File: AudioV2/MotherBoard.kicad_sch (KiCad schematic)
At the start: 50 parts, among them J201 +15/-15/A_GND out, J202 PD module in (1=GND 2=+12V), SW402 PWR SW, SW501 DEST L (PHONE/MUTE/LINE), SW502 DEST R (PHONE/MUTE/LINE), U201 REC10K-2415DAW/H2, U202 L7809CV +9V, U402 PT2314-D, U403 BP5293-50 +5V

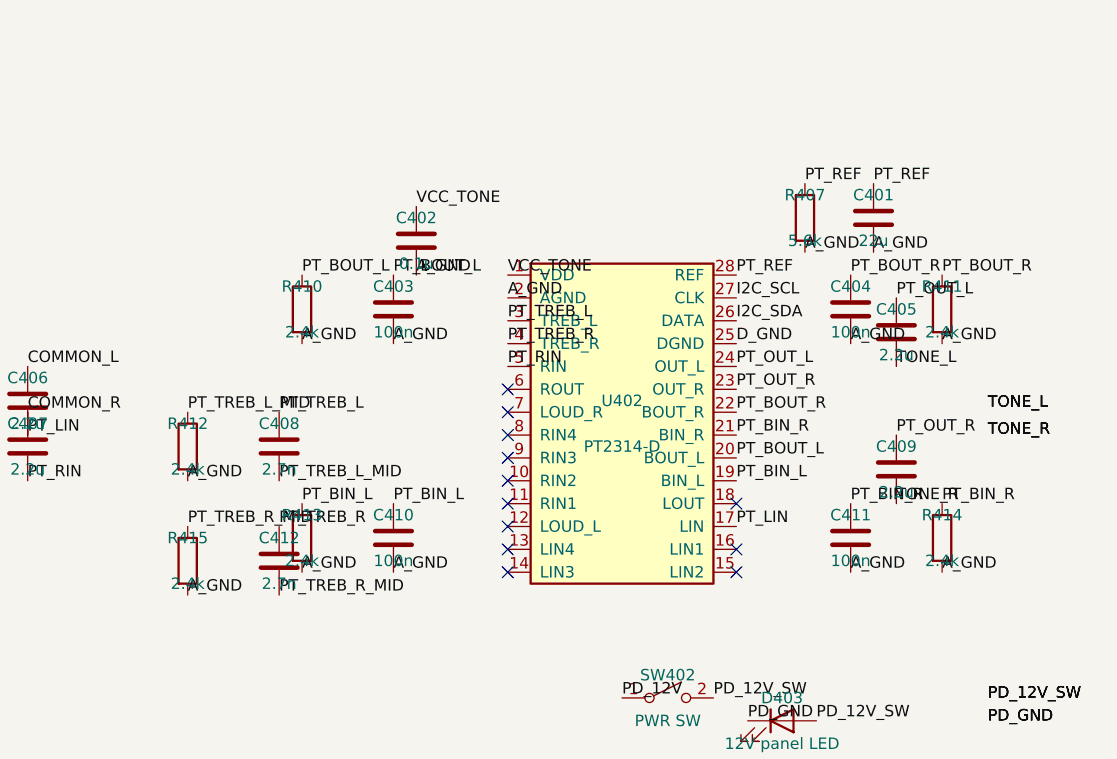
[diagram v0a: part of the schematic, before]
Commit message: AudioV2: PT2314E に切り替え、トーン網をデータシート通りに組み直した
無印 PT2314 は DigiKey に在庫が無く（フォーラムでモデレータ自身が調達困難と
回答し TDA7440 を代替に挙げている）、LCSC / JLCPCB にあるのは PT2314E のみ。
E は "Improved and replace PT2314 and PT2314A" と明記され、28ピンの名前・番号は
無印と完全一致（I2C の 26/27 が DATA/CLK -> SDA/SCL に改名されただけ）。

切り替えにあたって外付け網をデータシートと突き合わせたところ、3箇所ずれていた。
値の一覧は合っていたが置き場所が入れ替わっていた。2.4k は本来「使わないセレクタ
入力の直列抵抗」、5.6k は「低音網の集約点」。

  低音  DS: BOUT -[100n]-+-[5.6k]- GND
                BIN  -[100n]-+          （1点に集約）
        旧: BOUT/BIN が各自 100n と 2.4k で別々に GND。集約点が無く
            BIN->BASS->BOUT の外付け帰還路が成立していなかった
  高音  DS: TREB -[2.7n]- GND
        旧: TREB -[2.7n]-[2.4k]- GND（直列抵抗が余分）
  REF   DS: REF -[22u]- GND
        旧: REF -[22u]- GND に加えて 5.6k で GND へ（内部基準を引いていた）

無印 PT2314 のアプリケーション回路も同じ網なので、E への切り替えとは独立の誤り。

素材 legacy/ControlPanelAnalog.kicad_sch を編集して再生成した。この素材は
ワイヤを持たずラベルをピン先へ直置きする方式なので、配線変更はラベルの
張り替えで足りる。prune() は使っていない（このシートでもラベルを浮きと
誤認して落とすため）。消した部品のラベルはピン先座標で特定して消した。

  R410/R411  2.4k -> 5.6k、集約点 PT_BASS_L/R へ移動
  R407/R412/R413/R414/R415  削除
  C403/C410/C404/C411  GND 側を集約点へ
  C408/C412  中間ノードをやめて直接 A_GND へ
  U402 Value  PT2314-D -> PT2314E

フットプリントは設定していない。SOP-28 300mil だが、入手したDS抜粋に外形寸法が
無く SOIC-28W_7.5x17.9 と 7.5x18.7 のどちらか決められない。誤った値を入れると
「未設定」という目印が消えるので B5 で実物を見てから付ける。

検証:
  erc         17 件（変化なし。新規違反なし）
  netlist     部品 369 / 重複 0（抵抗5本減で 374 -> 369）
  dangling    0 本
  check_sexpr 13 ファイル / 問題 0
  roundtrip   6/6 OK
  再生成      2回目でバイト一致

CLAUDE.md の期待値表と NOW.md も更新した。

Co-Authored-By: Claude Opus 5 <noreply@anthropic.com>
Claude-Session: https://claude.ai/code/session_01VCArLcCGbMGgxvWJ5HFJiY
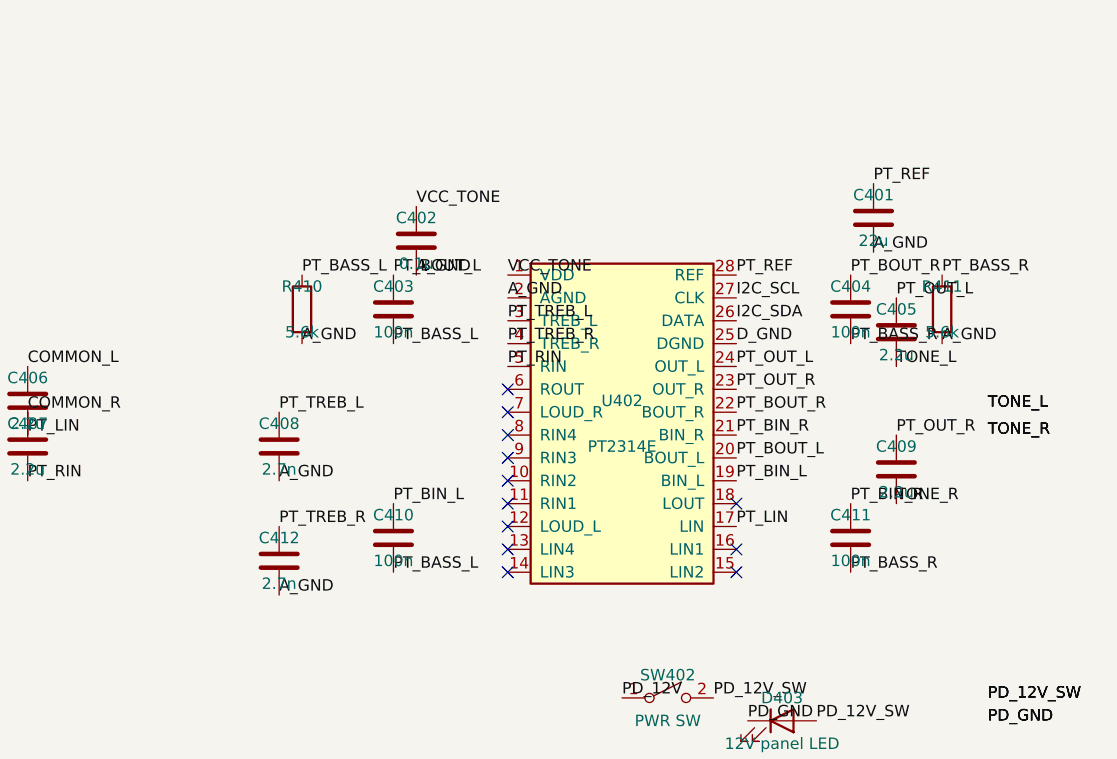
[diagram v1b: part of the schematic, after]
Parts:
- removed R407: 5.6k, symbol Device:R
- removed R412, R413, R414, R415: 2.4k, symbol Device:R
- R410, R411: value 2.4k -> 5.6k
- U402: value PT2314-D -> PT2314E
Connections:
- net PT_TREB_L_MID is gone; now on net A_GND: C408.2
- net PT_TREB_R_MID is gone; now on net A_GND: C412.2
- net A_GND: no longer C403.2, C404.2, C410.2, C411.2
- net PT_BOUT_L: no longer R410.1
- net PT_BOUT_R: no longer R411.1
- new net PT_BASS_L: C403.2, C410.2, R410.1
- new net PT_BASS_R: C404.2, C411.2, R411.1

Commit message: AudioV2: U402 のフットプリントを SOIC-28W_7.5x17.9mm に設定した
JLCPCB の Footprint Manager が出す LCSC の型は
SOP-28_L17.9-W7.5-P1.27-LS10.3 で、外形 17.9 x 7.5・ピッチ 1.27。
KiCad の Package_SO:SOIC-28W_7.5x17.9mm_P1.27mm と一致する。

パッドの伸ばし方だけ違うが、どちらもリードスパン 10.3mm を覆う:

            パッド中心間   パッド寸法      覆う範囲(x)
  LCSC      9.915          0.630 x 1.615   4.150 .. 5.765
  KiCad     9.300          0.600 x 2.050   3.625 .. 5.675
  リード足                                 約 4.35 .. 5.15

KiCad 側は IPC-7351 準拠でヒール側が広い。実装性はどちらでも問題ない。

フットプリント未設定は 45 -> 39。内訳は U402 を設定したぶん 1 個と、
前のコミットで消した抵抗 5 本（R407/R412/R413/R414/R415）がいずれも
未設定組だったぶん。

検証:
  erc         17 件（変化なし）
  netlist     部品 369 / 重複 0（変化なし）
  check_sexpr 13 ファイル / 問題 0
  roundtrip   6/6 OK

Co-Authored-By: Claude Opus 5 <noreply@anthropic.com>
Claude-Session: https://claude.ai/code/session_01VCArLcCGbMGgxvWJ5HFJiY
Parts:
- U402: footprint (none) -> Package_SO:SOIC-28W_7.5x17.9mm_P1.27mm
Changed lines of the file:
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@@
 			)
 		)
-		(property "Footprint" ""
+		(property "Footprint" "Package_SO:SOIC-28W_7.5x17.9mm_P1.27mm"
 			(at 355.6 0 0)
 			(hide yes)

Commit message: AudioV2: 母板のフットプリント 23 個を設計内の前例に合わせて埋めた（39 -> 16）
B5 の下ごしらえ。前例のあるものだけを埋め、判断が要るものには触っていない。

  積セラ 1206     C202/204/206/208/402, C403/404/410/411, C408/412
                  設計で 85 回使われている流儀に合わせた
  抵抗 1206       R410/411（同 128 回）
  フィルム        C405/406/407/409（2.2u）
                  PT2314 の入出力結合で音声が通る。設計内の C601「2.2uF film」と
                  同じ footprint に揃えた。セラミックは電圧で容量が変わるので
                  結合位置に置くと歪む（ユーザー判断 2026-09-07）
  電解            C201/205/207(47u) -> D8.0/P3.50（C1610・C1621 と同じ）
                  C401(22u)         -> D6.3/P2.50（C1630 と同じ）
                  C203(10u)         -> D5.0/P2.00（C1635「10uF 50V」と同じ）
  DC-DC           U403 -> Library:BP5293-50_ROHM_SIP-3
                  U1607 が同一部品で同じ footprint

素材（legacy/ControlPanelAnalog 15個・legacy/PowerModule 8個）を編集して再生成した。

**残り 16 個には触っていない。** 性質が2つに分かれる:

  パネル部品 6（RV501/502・SW501/502/1601・SW402）
    KiCad にもプロジェクトの Audio/Library.pretty にも footprint が無い。
    Alps は RK097/RK09K しかなく RK27 は別物。C&K 7000 系トグルも無い。
    データシートから新規に作る作業になる。
    さらに SW501/502/1601 は現物1個の 3PDT を3シンボルで表しているので、
    3つ全部に footprint を入れると PCB にスイッチが3個並ぶ。1個化が要る。

  調達判断待ち 10（D403・F201/202/203・J201/202・J_HP501・J_LINE501・
    J_RAIL501・U202）

検証:
  未設定      39 -> 16
  netlist     部品 370 / 重複 0（変化なし）
  erc         17 件（変化なし）
  check_sexpr 13 ファイル / 問題 0
  roundtrip   6/6 OK
  再生成      2回目でバイト一致

Co-Authored-By: Claude Opus 5 <noreply@anthropic.com>
Claude-Session: https://claude.ai/code/session_01VCArLcCGbMGgxvWJ5HFJiY
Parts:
- C201, C205, C207: footprint (none) -> Capacitor_THT:CP_Radial_D8.0mm_P3.50mm
- C202, C204, C206, C208, C402, C403, C404, C408, C410, C411, C412: footprint (none) -> Capacitor_SMD:C_1206_3216Metric_Pad1.33x1.80mm_HandSolder
- C203: footprint (none) -> Capacitor_THT:CP_Radial_D5.0mm_P2.00mm
- C401: footprint (none) -> Capacitor_THT:CP_Radial_D6.3mm_P2.50mm
- C405, C406, C407, C409: footprint (none) -> Capacitor_THT:C_Rect_L7.2mm_W2.5mm_P5.00mm_FKS2_FKP2_MKS2_MKP2
- R410, R411: footprint (none) -> Resistor_SMD:R_1206_3216Metric_Pad1.30x1.75mm_HandSolder
- U403: footprint (none) -> Library:BP5293-50_ROHM_SIP-3
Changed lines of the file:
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@@
 			)
 		)
-		(property "Footprint" ""
+		(property "Footprint" "Capacitor_THT:CP_Radial_D5.0mm_P2.00mm"
 			(at 22.86 10.16 0)
 			(hide yes)
@@
 			)
 		)
-		(property "Footprint" ""
+		(property "Footprint" "Capacitor_THT:CP_Radial_D8.0mm_P3.50mm"
 			(at -1.27 20.32 0)
 			(hide yes)
@@
 			)
 		)
-		(property "Footprint" ""
+		(property "Footprint" "Capacitor_SMD:C_1206_3216Metric_Pad1.33x1.80mm_HandSolder"
 			(at -62.23 21.59 0)
 			(hide yes)
@@
 			)
 		)
-		(property "Footprint" ""
+		(property "Footprint" "Capacitor_SMD:C_1206_3216Metric_Pad1.33x1.80mm_HandSolder"
 			(at 3.81 10.16 0)
 			(hide yes)
@@
 			)
 		)
-		(property "Footprint" ""
+		(property "Footprint" "Capacitor_SMD:C_1206_3216Metric_Pad1.33x1.80mm_HandSolder"
 			(at -7.62 17.78 0)
 			(hide yes)
@@
 			)
 		)
-		(property "Footprint" ""
+		(property "Footprint" "Capacitor_SMD:C_1206_3216Metric_Pad1.33x1.80mm_HandSolder"
 			(at -7.62 25.4 0)
 			(hide yes)
@@
 			)
 		)
-		(property "Footprint" ""
+		(property "Footprint" "Capacitor_THT:CP_Radial_D8.0mm_P3.50mm"
 			(at -1.27 17.78 0)
 			(hide yes)
@@
 			)
 		)
-		(property "Footprint" ""
+		(property "Footprint" "Capacitor_THT:CP_Radial_D8.0mm_P3.50mm"
 			(at -8.89 31.75 0)
 			(hide yes)
@@
 			)
 		)
-		(property "Footprint" ""
+		(property "Footprint" "Capacitor_SMD:C_1206_3216Metric_Pad1.33x1.80mm_HandSolder"
 			(at 355.6 0 0)
 			(hide yes)
@@
 			)
 		)
-		(property "Footprint" ""
+		(property "Footprint" "Capacitor_SMD:C_1206_3216Metric_Pad1.33x1.80mm_HandSolder"
 			(at 355.6 0 0)
 			(hide yes)
@@
 			)
 		)
-		(property "Footprint" ""
+		(property "Footprint" "Capacitor_SMD:C_1206_3216Metric_Pad1.33x1.80mm_HandSolder"
 			(at 355.6 0 0)
 			(hide yes)
@@
 			)
 		)
-		(property "Footprint" ""
+		(property "Footprint" "Capacitor_SMD:C_1206_3216Metric_Pad1.33x1.80mm_HandSolder"
 			(at 355.6 0 0)
 			(hide yes)
@@
 			)
 		)
-		(property "Footprint" ""
+		(property "Footprint" "Capacitor_THT:C_Rect_L7.2mm_W2.5mm_P5.00mm_FKS2_FKP2_MKS2_MKP2"
 			(at 355.6 0 0)
 			(hide yes)
@@
 			)
 		)
-		(property "Footprint" ""
+		(property "Footprint" "Resistor_SMD:R_1206_3216Metric_Pad1.30x1.75mm_HandSolder"
 			(at 355.6 0 0)
 			(hide yes)
@@
 			)
 		)
-		(property "Footprint" ""
+		(property "Footprint" "Capacitor_SMD:C_1206_3216Metric_Pad1.33x1.80mm_HandSolder"
 			(at 355.6 0 0)
 			(hide yes)
@@
 			)
 		)
-		(property "Footprint" ""
+		(property "Footprint" "Capacitor_THT:CP_Radial_D6.3mm_P2.50mm"
 			(at 355.6 0 0)
 			(hide yes)
@@
 			)
 		)
-		(property "Footprint" ""
+		(property "Footprint" "Capacitor_THT:C_Rect_L7.2mm_W2.5mm_P5.00mm_FKS2_FKP2_MKS2_MKP2"
 			(at 355.6 0 0)
 			(hide yes)
@@
 			)
 		)
-		(property "Footprint" ""
+		(property "Footprint" "Library:BP5293-50_ROHM_SIP-3"
 			(at 355.6 0 0)
 			(hide yes)
@@
 			)
 		)
-		(property "Footprint" ""
+		(property "Footprint" "Capacitor_SMD:C_1206_3216Metric_Pad1.33x1.80mm_HandSolder"
 			(at 355.6 0 0)
 			(hide yes)
@@
 			)
 		)
-		(property "Footprint" ""
+		(property "Footprint" "Capacitor_THT:C_Rect_L7.2mm_W2.5mm_P5.00mm_FKS2_FKP2_MKS2_MKP2"
 			(at 355.6 0 0)
 			(hide yes)
@@
 			)
 		)
-		(property "Footprint" ""
+		(property "Footprint" "Capacitor_THT:C_Rect_L7.2mm_W2.5mm_P5.00mm_FKS2_FKP2_MKS2_MKP2"
 			(at 355.6 0 0)
 			(hide yes)
@@
 			)
 		)
-		(property "Footprint" ""
+		(property "Footprint" "Capacitor_SMD:C_1206_3216Metric_Pad1.33x1.80mm_HandSolder"
 			(at 355.6 0 0)
 			(hide yes)
@@
 			)
 		)
-		(property "Footprint" ""
+		(property "Footprint" "Resistor_SMD:R_1206_3216Metric_Pad1.30x1.75mm_HandSolder"
 			(at 355.6 0 0)
 			(hide yes)

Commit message: AudioV2: パネル部品6個をヘッダのフットプリントにした（16 -> 10）
PARTS.md がヘッダ構成まで既に指定していた。それに従っただけで、新しい判断は
入れていない。

  PARTS.md:5    RV / SW_DEST / ENC / PWR SW は パネル実装。基板はヘッダ＋リード
  PARTS.md:173  RV は基板 6P ヘッダ（Device:R_Potentiometer_Dual ピン番号のまま）
  PARTS.md:141  SW_DEST は 現物端子 -> 基板ヘッダ（音声 2x4 + センス 1x3）

  RV501/502     PinHeader_1x06   シンボルのピン 1-6 がそのままヘッダのピン
  SW501/502     PinHeader_1x04   PARTS.md §2.1 の SW601-1..4 / SW602-1..4 に対応
  SW1601        PinHeader_1x04   同じ並び。pin2(MUTE) は基板側で未使用
  SW402         PinHeader_1x02   SPST

ポットの品種（Alps RK27 か RK097 か Alpha RD901 か）は決めていない。
PARTS.md が「RK097 でも回路は同一」「A50k デュアルならピン互換で可」と
書いており、電気的な要件は A カーブ・50k・2連だけ。**ヘッダなので基板側は
品種に依存しない**。入手性と性能で選ぶ調達判断として残す（ユーザー判断 2026-09-07）。

⚠ PARTS.md の「音声 2x4」は 2行4列ではなく「4ピンを2組」と読んだ。同 §2.1 の
ピン対応表が SW601-1..4 / SW602-1..4 と別々に並べており、シンボルも2つに
分かれているため。2行4列の1個を意図していたなら要修正。

副次的に、Cursor 査読の「DEST の 3PDT が自動 BOM 上で現物3個に見える」も解ける。
基板に載るのはヘッダ3個（実際に3個要る）で、スイッチ本体はパネル部品として
基板 BOM に出ないのが正しい形。

なお PARTS.md §2.1 のピン対応表は SW601-3 をコモン（AMP_SEL_L）としており、
今日 SW1601 で直した割り当て（pin3=コモン）と一致していた。

検証:
  未設定      16 -> 10（残りは D403・F201/202/203・J201/202・J_HP501・
              J_LINE501・J_RAIL501・U202。すべて調達判断待ち）
  netlist     部品 370 / 重複 0（変化なし）
  erc         17 件（変化なし）
  check_sexpr 13 ファイル / 問題 0
  roundtrip   6/6 OK
  再生成      2回目でバイト一致

Co-Authored-By: Claude Opus 5 <noreply@anthropic.com>
Claude-Session: https://claude.ai/code/session_01VCArLcCGbMGgxvWJ5HFJiY
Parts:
- RV501, RV502: footprint (none) -> Connector_PinHeader_2.54mm:PinHeader_1x06_P2.54mm_Vertical
- SW402: footprint (none) -> Connector_PinHeader_2.54mm:PinHeader_1x02_P2.54mm_Vertical
- SW501, SW502: footprint (none) -> Connector_PinHeader_2.54mm:PinHeader_1x04_P2.54mm_Vertical
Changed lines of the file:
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@@
 			)
 		)
-		(property "Footprint" ""
+		(property "Footprint" "Connector_PinHeader_2.54mm:PinHeader_1x06_P2.54mm_Vertical"
 			(at 0 111.76 0)
 			(hide yes)
@@
 			)
 		)
-		(property "Footprint" ""
+		(property "Footprint" "Connector_PinHeader_2.54mm:PinHeader_1x04_P2.54mm_Vertical"
 			(at -26.67 113.03 0)
 			(hide yes)
@@
 			)
 		)
-		(property "Footprint" ""
+		(property "Footprint" "Connector_PinHeader_2.54mm:PinHeader_1x06_P2.54mm_Vertical"
 			(at 0 120.65 0)
 			(hide yes)
@@
 			)
 		)
-		(property "Footprint" ""
+		(property "Footprint" "Connector_PinHeader_2.54mm:PinHeader_1x04_P2.54mm_Vertical"
 			(at -26.67 114.3 0)
 			(hide yes)
@@
 			)
 		)
-		(property "Footprint" ""
-			(at 355.6 0 0)
-			(hide yes)
+		(property "Footprint" "Connector_PinHeader_2.54mm:PinHeader_1x02_P2.54mm_Vertical"
+			(at 355.6 0 0)
+			(hide yes)

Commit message: AudioV2: 端子台5個を Phoenix MKDS-1,5 にした（10 -> 5）
ユーザー判断（2026-09-07）。PARTS.md:211 が板間の端子台に Phoenix MKDS-1,5
系を指定しており、計測基板の J1601(2P) / J1603(3P) に既に同じ footprint が
入っている。その前例に合わせた。

  J201       1x03  +15/-15/A_GND out
  J202       1x02  PD module in
  J_HP501    1x02  to Audio HP Buffer
  J_LINE501  1x02  LINE OUT
  J_RAIL501  1x03  RAIL IN

J_HP501 / J_LINE501 / J_RAIL501 は元から Connector:Screw_Terminal_01xNN
シンボルなので端子台が自然。J201 / J202 は Conn_01xNN_Pin（汎用ピン）だが、
板間の電源なので同じ系に揃えた。

残り5個は性質が違うので手を付けていない:
  D403             12V パネル LED。直列抵抗の有無が未決（DECISIONS の既知項目）
  F201             T1.6A slow 5x20。ヒューズホルダの品種
  F202/F203        PPTC。MPN 未確定（直流抵抗とディレーティングが決まらない）
  U202             L7809CV TO-220。実装向き（垂直/水平・放熱器）が機構判断

検証:
  未設定      10 -> 5
  netlist     部品 370 / 重複 0（変化なし）
  erc         17 件（変化なし）
  check_sexpr 13 ファイル / 問題 0
  roundtrip   6/6 OK
  再生成      2回目でバイト一致

Co-Authored-By: Claude Opus 5 <noreply@anthropic.com>
Claude-Session: https://claude.ai/code/session_01VCArLcCGbMGgxvWJ5HFJiY
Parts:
- J201, J_RAIL501: footprint (none) -> TerminalBlock_Phoenix:TerminalBlock_Phoenix_MKDS-1,5-3-5.08_1x03_P5.08mm_Horizontal
- J202, J_HP501, J_LINE501: footprint (none) -> TerminalBlock_Phoenix:TerminalBlock_Phoenix_MKDS-1,5-2-5.08_1x02_P5.08mm_Horizontal
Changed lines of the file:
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@@
 			)
 		)
-		(property "Footprint" ""
+		(property "Footprint" "TerminalBlock_Phoenix:TerminalBlock_Phoenix_MKDS-1,5-2-5.08_1x02_P5.08mm_Horizontal"
 			(at 26.67 -5.08 0)
 			(hide yes)
@@
 			)
 		)
-		(property "Footprint" ""
+		(property "Footprint" "TerminalBlock_Phoenix:TerminalBlock_Phoenix_MKDS-1,5-3-5.08_1x03_P5.08mm_Horizontal"
 			(at -59.69 6.35 0)
 			(hide yes)
@@
 			)
 		)
-		(property "Footprint" ""
+		(property "Footprint" "TerminalBlock_Phoenix:TerminalBlock_Phoenix_MKDS-1,5-2-5.08_1x02_P5.08mm_Horizontal"
 			(at 8.89 115.57 0)
 			(hide yes)
@@
 			)
 		)
-		(property "Footprint" ""
+		(property "Footprint" "TerminalBlock_Phoenix:TerminalBlock_Phoenix_MKDS-1,5-2-5.08_1x02_P5.08mm_Horizontal"
 			(at 8.89 111.76 0)
 			(hide yes)
@@
 			)
 		)
-		(property "Footprint" ""
+		(property "Footprint" "TerminalBlock_Phoenix:TerminalBlock_Phoenix_MKDS-1,5-3-5.08_1x03_P5.08mm_Horizontal"
 			(at -13.97 49.53 0)
 			(hide yes)

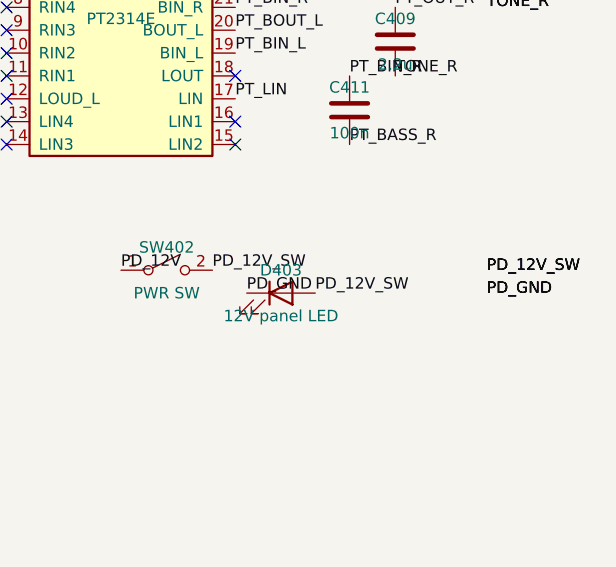
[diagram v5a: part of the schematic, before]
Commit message: AudioV2: 残り5個のフットプリントを埋めた（5 -> 0）。D403 に直列抵抗 R401
フットプリント未設定 0 個。これで netlist 上の 371 部品すべてに footprint が付いた。

- F201/F202/F203 … Resistor_THT:R_Axial_DIN0411_L9.9mm_D3.6mm_P12.70mm_Horizontal
  設計内の F1601/F1602/F1603 と同じリード品に揃えた。ピッチが3種類に散らばる
  より、入手性のいい 5x20mm 相当の軸形1種に寄せたほうが調達が楽になる
- U202 … Package_TO_SOT_THT:TO-220-3_Vertical
  垂直立て。放熱器の要否と向きは PCB を起こすとき（B5）に決め直す
- D403 … LED_THT:LED_D5.0mm（設計内の D1610/D1611 と同じ）

D403 は PD_12V_SW に直付けだったので、電流制限の 2.2k を直列に入れた:

    PD_12V_SW ─[R401 2.2k]─ LED_12V_A ─[D403]─ PD_GND

抵抗なしだと LED の Vf ばらつきがそのまま電流に出る。12V で Vf 2.0V 想定なら
約 4.5mA。部品数 370 -> 371（CLAUDE.md の期待値も更新）。

生成シートは直接触らず、素材の legacy/ControlPanelAnalog.kicad_sch と
legacy/PowerModule.kicad_sch を編集して build_daughter -> build_motherboard で
再生成した。

検証:
  check_sexpr.py -q AudioV2        13 ファイル / 問題 0
  kicad-run.sh erc                 17 件（変化なし）
  kicad-run.sh netlist             部品 371 個・重複 0・footprint 未設定 0
  sch_import.py --roundtrip        6/6 OK
  再生成の冪等性                    バイト一致

⚠ PARTS.md の「音声 2×4」は「4ピンのヘッダを2組」と読んで 2 x PinHeader_1x04 に
した。2行4列（PinHeader_2x04）のつもりだったなら直す必要がある。

Co-Authored-By: Claude Opus 5 <noreply@anthropic.com>
Claude-Session: https://claude.ai/code/session_01VCArLcCGbMGgxvWJ5HFJiY
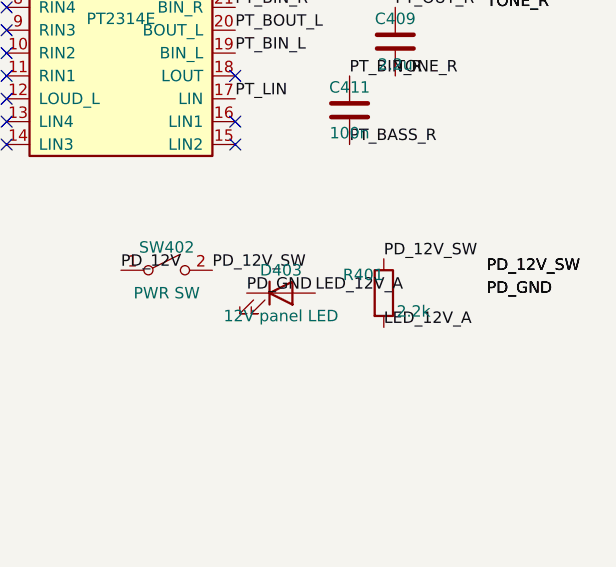
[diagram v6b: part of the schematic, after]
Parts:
- added R401: 2.2k, Resistor_SMD:R_1206_3216Metric_Pad1.30x1.75mm_HandSolder, symbol Device:R
- D403: footprint (none) -> LED_THT:LED_D5.0mm
- F201, F202, F203: footprint (none) -> Resistor_THT:R_Axial_DIN0411_L9.9mm_D3.6mm_P12.70mm_Horizontal
- U202: footprint (none) -> Package_TO_SOT_THT:TO-220-3_Vertical
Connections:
- net PD_12V_SW: now also R401.1; no longer D403.2 (A)
- new net LED_12V_A: D403.2 (A), R401.2
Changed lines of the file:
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@@
 			)
 		)
-		(property "Footprint" ""
+		(property "Footprint" "Package_TO_SOT_THT:TO-220-3_Vertical"
 			(at 0 11.43 0)
 			(hide yes)
@@
 			)
 		)
-		(property "Footprint" ""
+		(property "Footprint" "Resistor_THT:R_Axial_DIN0411_L9.9mm_D3.6mm_P12.70mm_Horizontal"
 			(at -12.7 45.72 0)
 			(hide yes)
@@
 			)
 		)
-		(property "Footprint" ""
+		(property "Footprint" "Resistor_THT:R_Axial_DIN0411_L9.9mm_D3.6mm_P12.70mm_Horizontal"
 			(at -12.7 45.72 0)
 			(hide yes)
@@
 			)
 		)
-		(property "Footprint" ""
+		(property "Footprint" "Resistor_THT:R_Axial_DIN0411_L9.9mm_D3.6mm_P12.70mm_Horizontal"
 			(at -12.7 45.72 0)
 			(hide yes)
@@
 		)
 	)
-	(label "PD_12V_SW"
+	(label "LED_12V_A"
 		(at 537.21 152.4 0)
 		(effects
@@
 			)
 		)
-		(property "Footprint" ""
+		(property "Footprint" "LED_THT:LED_D5.0mm"
 			(at 355.6 0 0)
 			(hide yes)
@@
 		)
 	)
+	(symbol
+		(lib_id "Device:R")
+		(at 544.83 152.4 0)
+		(unit 1)
+		(body_style 1)
+		(exclude_from_sim no)
+		(in_bom yes)
+		(on_board yes)
+		(in_pos_files yes)
+		(dnp no)
+		(property "Reference" "R401"
+			(at 542.544 150.368 0)
+			(show_name no)
+			(do_not_autoplace no)
+			(effects
+				(font
+					(size 1.27 1.27)
+				)
+			)
+		)
+		(property "Value" "2.2k"
+			(at 548.132 154.432 0)
+			(show_name no)
+			(do_not_autoplace no)
+			(effects
+				(font
+					(size 1.27 1.27)
+				)
+			)
+		)
+		(property "Footprint" "Resistor_SMD:R_1206_3216Metric_Pad1.30x1.75mm_HandSolder"
+			(at 544.83 152.4 0)
+			(hide yes)
+			(show_name no)
+			(do_not_autoplace no)
+			(effects
+				(font
+					(size 1.27 1.27)
+				)
+			)
+		)
+		(property "Datasheet" ""
+			(at 544.83 152.4 0)
+			(hide yes)
+			(show_name no)
+			(do_not_autoplace no)
+			(effects
+				(font
+					(size 1.27 1.27)
+				)
+			)
+		)
+		(property "Description" "D403(12V パネル LED)の直列抵抗。素の LED でも 12V 直結で壊れないようにする。(12-Vf2)/2.2k = 約 4.5mA。抵抗内蔵の 12V LED を挿しても点く（やや暗い）。"
+			(at 544.83 152.4 0)
+			(hide yes)
+			(show_name no)
+			(do_not_autoplace no)
+			(effects
+				(font
+					(size 1.27 1.27)
+				)
+			)
+		)
+		(pin "1"
+		)
+		(pin "2"
+		)
+		(instances
+			(project "AudioV2Case"
+				(path "/a1000001-0001-4001-8001-000000000001/a1000012-0012-4012-8012-000000000012"
+					(reference "R401")
+					(unit 1)
+				)
+			)
+		)
+	)
+	(label "PD_12V_SW"
+		(at 544.83 148.59 0)
+		(effects
+			(font
+				(size 1.27 1.27)
+			)
+			(justify left bottom)
+		)
+	)
+	(label "LED_12V_A"
+		(at 544.83 156.21 0)
+		(effects
+			(font
+				(size 1.27 1.27)
+			)
+			(justify left bottom)
+		)
+	)
